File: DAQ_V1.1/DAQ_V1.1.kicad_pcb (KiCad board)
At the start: 2 copper layers, 105.5 x 100 mm, 20 parts, among them J1 Screw_Terminal_01x02, J2 Screw_Terminal_01x04, J3 Screw_Terminal_01x04, J4 Screw_Terminal_01x04, J5 Screw_Terminal_01x04

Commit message: Added PT firmware and logging interface
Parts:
- moved ? 0.90 mm to (156.5, 88.2)
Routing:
- net Net-(A2-D51_MOSI): track 135.3 -> 134.7 mm
- net Net-(A2-D50_MISO): track 133.9 -> 133.4 mm
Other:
- board text added: "G1"
- board text added: "G2"
- board text added: "G3"
- board text removed: "GND1"
- board text removed: "GND2"

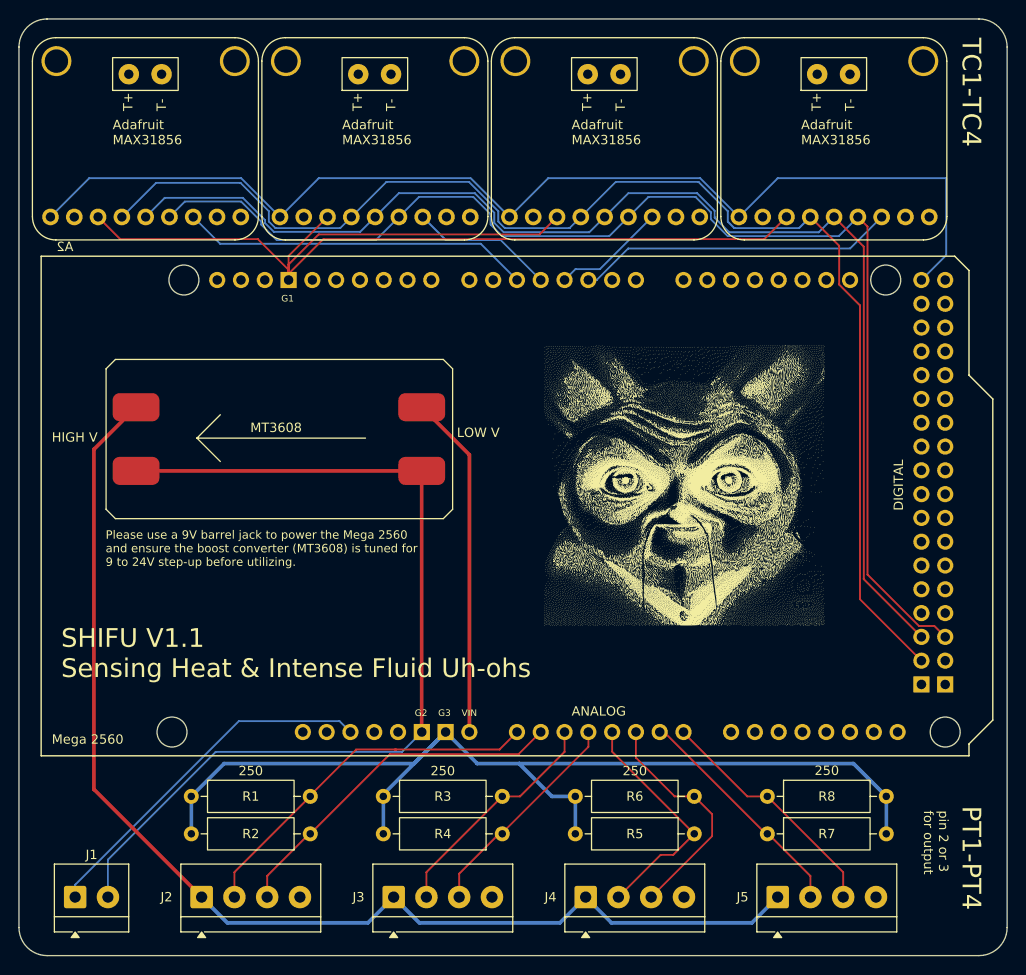
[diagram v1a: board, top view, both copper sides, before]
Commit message: Rework to firmware, interface + minor changes to PCB
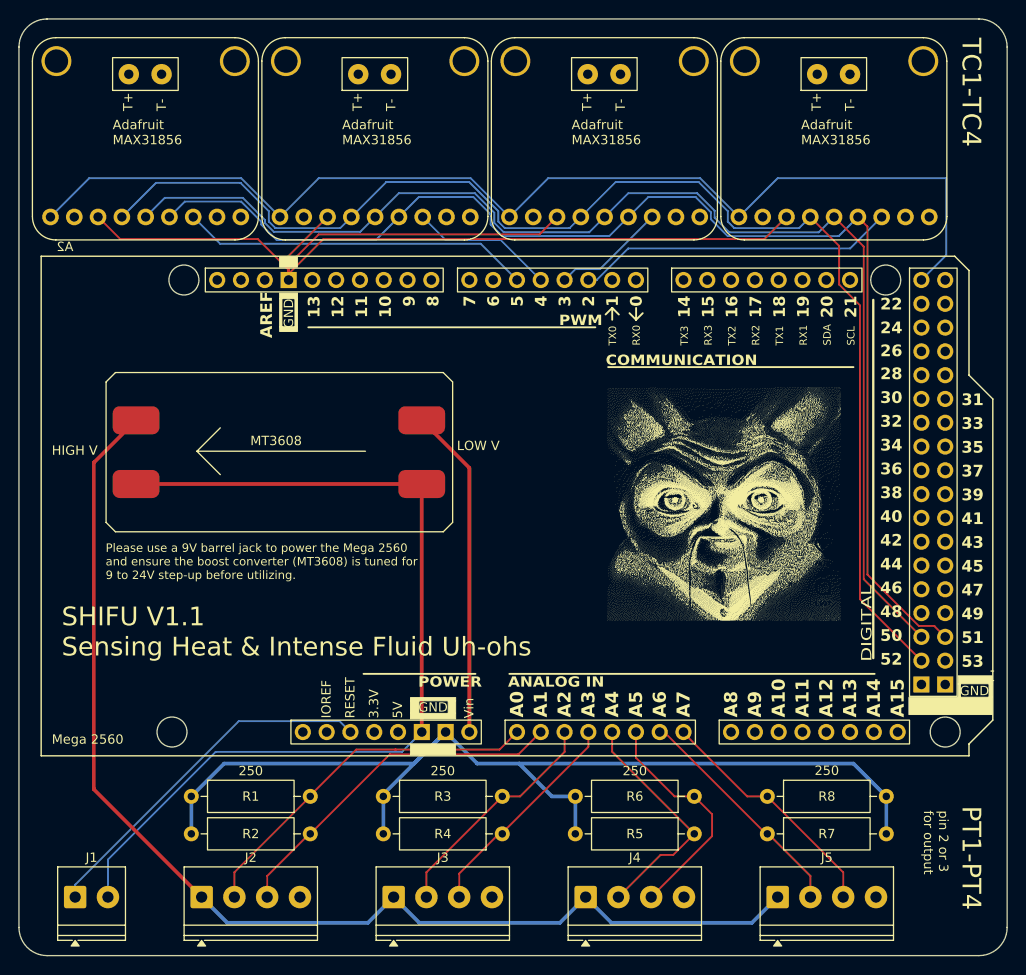
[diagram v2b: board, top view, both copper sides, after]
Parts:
- removed ?: LOGO, CustomLibrary:SHIFU_SS
- added G***: LOGO, CustomLibrary:SHIFU_SS, F.Cu at (160.8, 90.2)
- J1: footprint TerminalBlock_4Ucon:TerminalBlock_4Ucon_1x02_P3.50mm_Horizontal -> TerminalBlock_Phoenix:TerminalBlock_Phoenix_PT-1,5-2-3.5-H_1x02_P3.50mm_Horizontal
- J2, J3, J4, J5: footprint TerminalBlock_4Ucon:TerminalBlock_4Ucon_1x04_P3.50mm_Horizontal -> TerminalBlock_Phoenix:TerminalBlock_Phoenix_PT-1,5-4-3.5-H_1x04_P3.50mm_Horizontal
- U1, U2, U3, U4: footprint Adafruit MAX31856-import-fps:Max31856Pads -> CustomLibrary:Max31856Pads
- moved U5 1.40 mm to (113.5, 84.2)
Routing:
- net Net-(J2-Pin_1): track 127.3 -> 125.9 mm
- net GND2: track 101.5 -> 100.1 mm
- net Net-(U5-Vin+): track 36.8 -> 35.4 mm
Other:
- board text removed: "ANALOG"
- board text removed: "DIGITAL"
- board text removed: "G1"
- board text removed: "G2"
- board text removed: "G3"
- board text removed: "VIN"
